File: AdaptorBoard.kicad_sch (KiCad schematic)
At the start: 23 parts, among them J1 Conn_02x05_Odd_Even, SW1 SW_Push, SW2 SW_Push

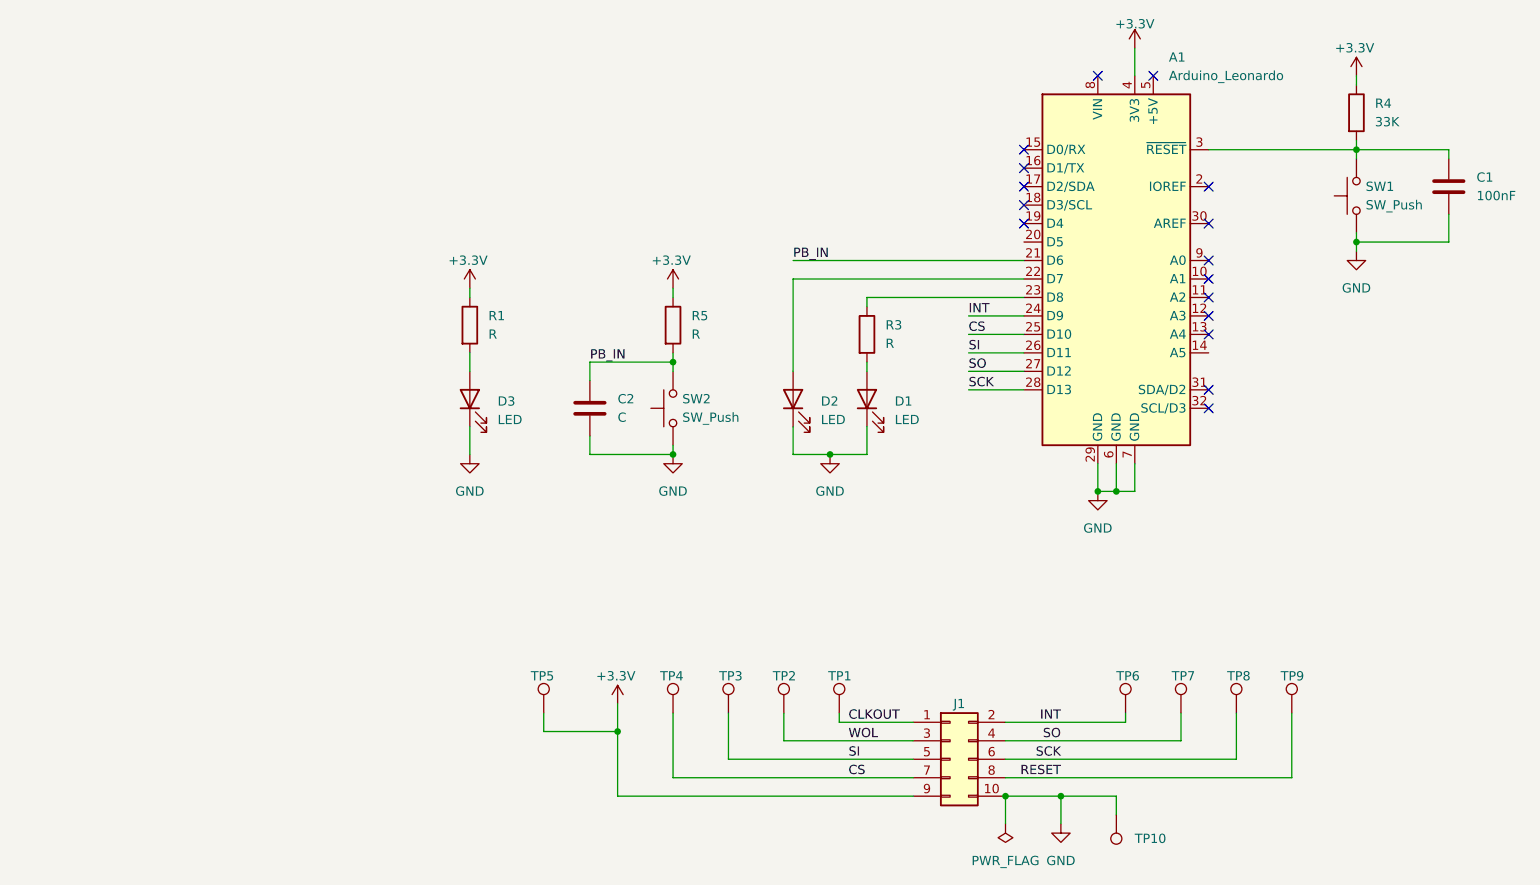
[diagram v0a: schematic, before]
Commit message: Add EEPROM. Change from Reset Push to input. Assign footprints and more improvements.
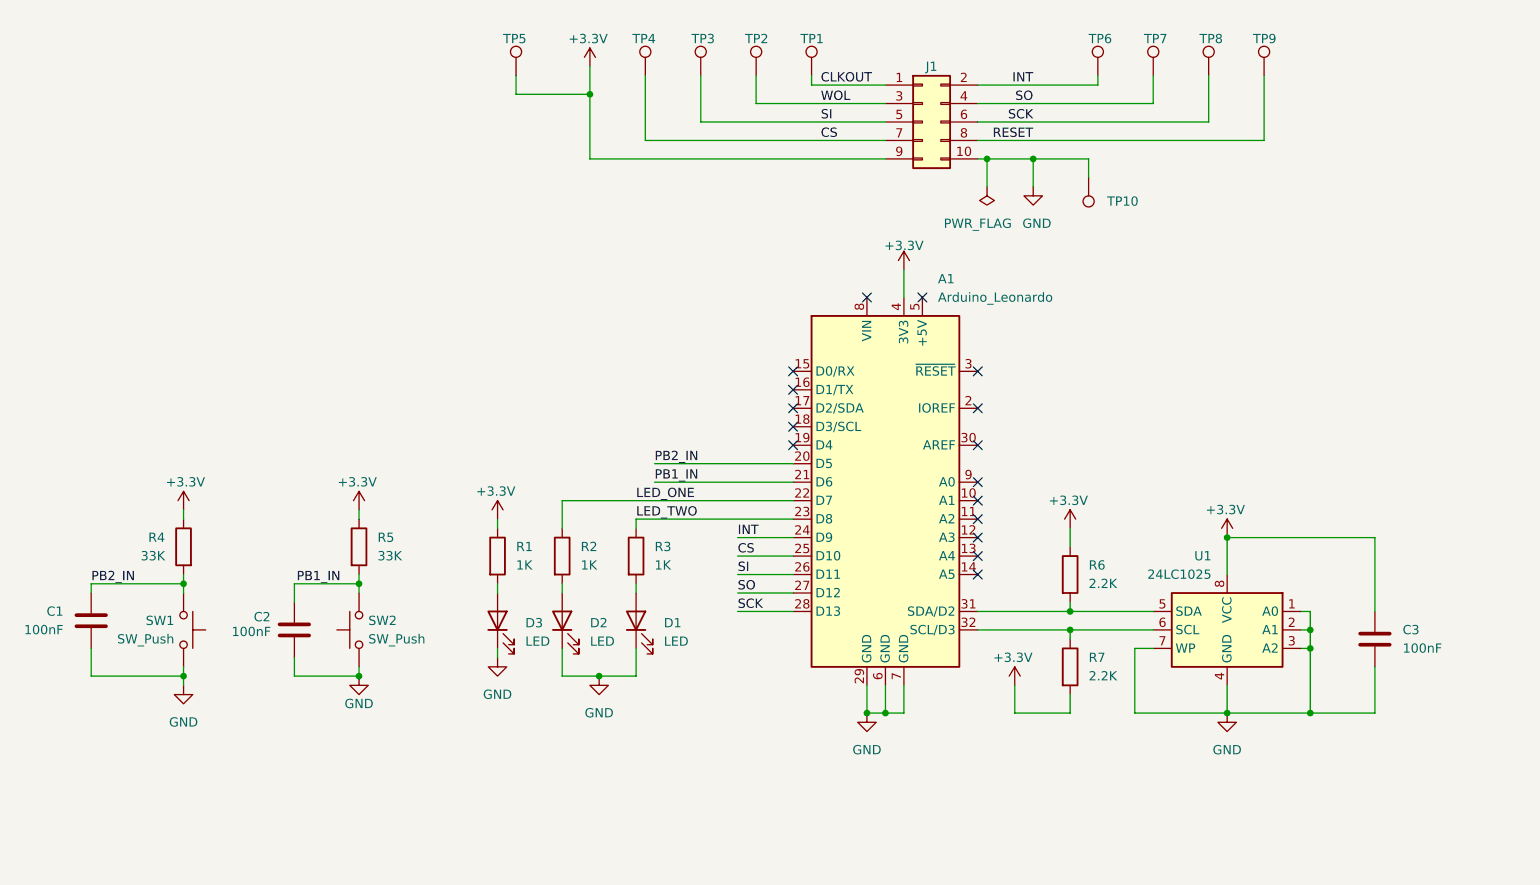
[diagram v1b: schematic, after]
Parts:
- added C3: 100nF, Capacitor_SMD:C_0603_1608Metric_Pad1.08x0.95mm_HandSolder, symbol Device:C
- added R2: 1K, Resistor_SMD:R_0603_1608Metric_Pad0.98x0.95mm_HandSolder, symbol Device:R
- added R6, R7: 2.2K, Resistor_SMD:R_0603_1608Metric_Pad0.98x0.95mm_HandSolder, symbol Device:R
- added U1: 24LC1025, Package_SO:SOIC-8_3.9x4.9mm_P1.27mm, symbol Memory_EEPROM:24LC1025
- C1: footprint (none) -> Capacitor_SMD:C_0603_1608Metric_Pad1.08x0.95mm_HandSolder
- C2: value C -> 100nF; footprint (none) -> Capacitor_SMD:C_0603_1608Metric_Pad1.08x0.95mm_HandSolder
- D1, D2, D3: footprint (none) -> LED_SMD:LED_0603_1608Metric_Pad1.05x0.95mm_HandSolder
- R1, R3: value R -> 1K; footprint (none) -> Resistor_SMD:R_0603_1608Metric_Pad0.98x0.95mm_HandSolder
- R4: footprint (none) -> Resistor_SMD:R_0603_1608Metric_Pad0.98x0.95mm_HandSolder
- R5: value R -> 33K; footprint (none) -> Resistor_SMD:R_0603_1608Metric_Pad0.98x0.95mm_HandSolder
- SW1, SW2: footprint (none) -> Button_Switch_SMD:SW_Tactile_SPST_NO_Straight_CK_PTS636Sx25SMTRLFS
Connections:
- net +3.3V: now also C3.1, R6.1, R7.2, U1.8 (VCC)
- net GND: now also C3.2, U1.1 (A0), U1.2 (A1), U1.3 (A2), U1.4 (GND), U1.7 (WP)
- net LED_TWO: now reaches A1.23 (D8), R3.1
- net PB2_IN: now reaches C1.1, R4.2, SW1.2
- net PB2_IN: now also A1.20 (D5); no longer A1.3 (~{RESET})
- net at D2.2 (A): now also R2.2; no longer A1.22 (D7)
- net at A1.31 (SDA/D2): now also R6.2, U1.5 (SDA)
- net at A1.32 (SCL/D3): now also R7.1, U1.6 (SCL)
- net PB_IN renamed PB1_IN
- new net LED_ONE: A1.22 (D7), R2.1
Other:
- company: (none) -> FEYTECH PTY LTD
- title: (none) -> ENC28J60 SHIELD
- moved on the sheet: A1, C1, C2, D1, D2, D3, J1, R1, R3, R4, R5, SW1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
